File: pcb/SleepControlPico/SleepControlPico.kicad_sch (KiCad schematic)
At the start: 27 parts, among them J1 Display, J2 USB_C_Receptacle_USB2.0, J3 Conn_01x03, J4 Photodiode, SW1 RotaryEncoder_Switch, SW2 Boot, U1 AMS1117-33, U2 ESP32-S3-MINI-1-N8, U3 USBLC6-2SC6

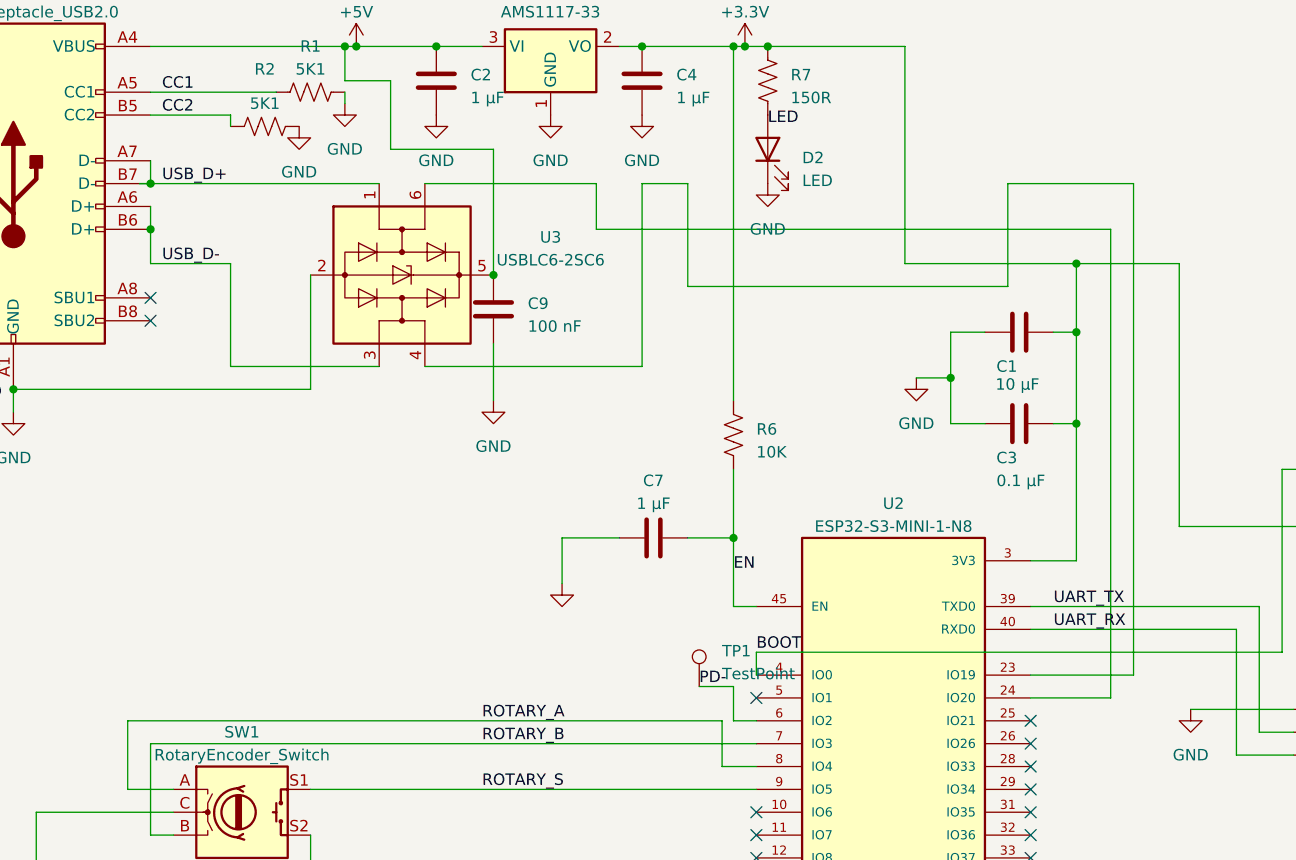
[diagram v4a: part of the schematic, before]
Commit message: Fix USB D+ and D- lines being switched
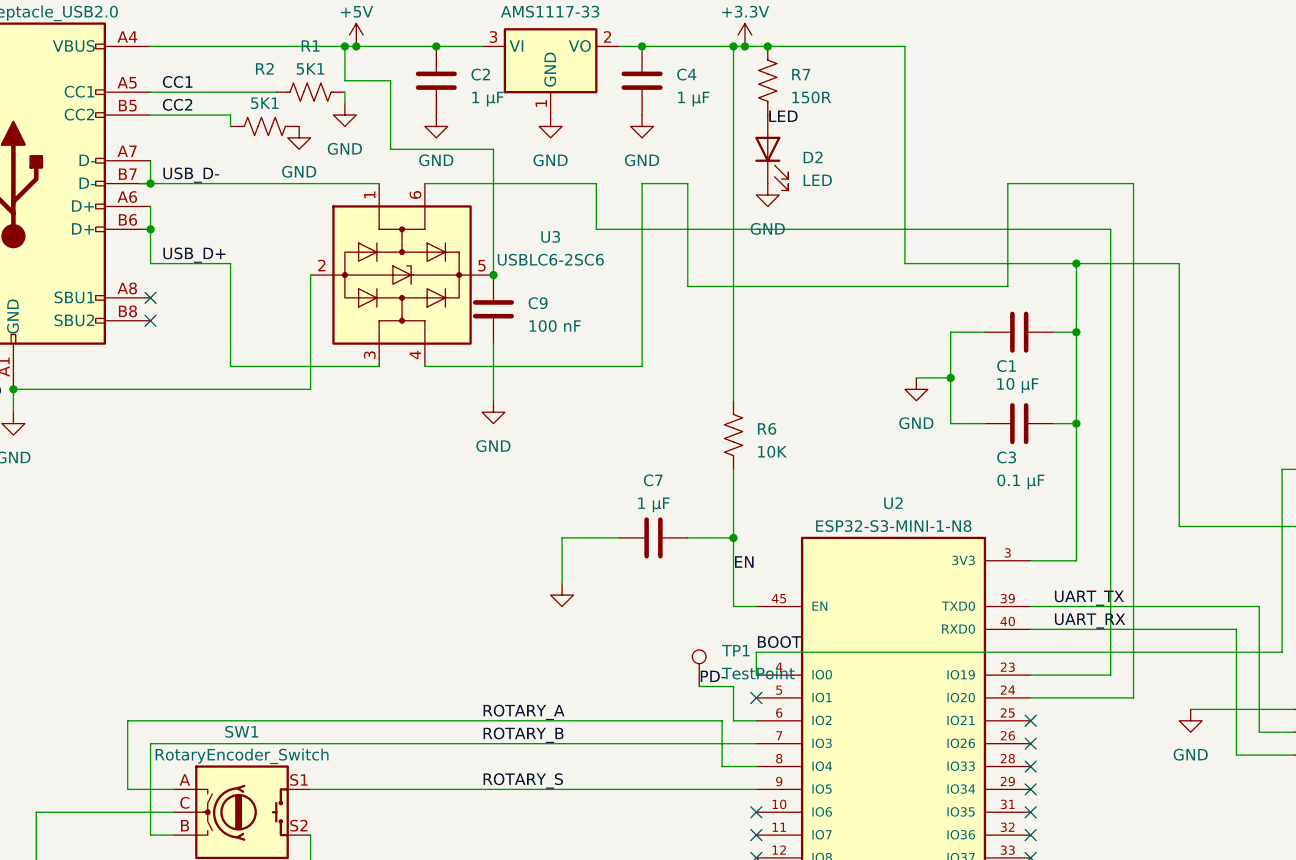
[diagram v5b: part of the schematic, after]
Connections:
- net USB_D+: now also J2.A6 (D+), J2.B6 (D+), U3.3 (I/O2); no longer J2.A7 (D-), J2.B7 (D-), U3.1 (I/O1)
- net USB_D-: now also J2.A7 (D-), J2.B7 (D-), U3.1 (I/O1); no longer J2.A6 (D+), J2.B6 (D+), U3.3 (I/O2)
- net at U2.23 (IO19): now also U3.6 (I/O1); no longer U3.4 (I/O2)
- net at U2.24 (IO20): now also U3.4 (I/O2); no longer U3.6 (I/O1)
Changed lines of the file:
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@@
     (stroke (width 0) (type default))
   )
-  (wire (pts (xy 157.48 49.53) (xy 157.48 101.6))
+  (wire (pts (xy 157.48 49.53) (xy 157.48 99.06))
     (stroke (width 0) (type default))
   )
@@
     (stroke (width 0) (type default))
   )
-  (wire (pts (xy 157.48 101.6) (xy 148.59 101.6))
-    (stroke (width 0) (type default))
-  )
   (wire (pts (xy 189.23 82.55) (xy 190.5 82.55))
     (stroke (width 0) (type default))
@@
     (stroke (width 0) (type default))
   )
-  (wire (pts (xy 160.02 99.06) (xy 148.59 99.06))
-    (stroke (width 0) (type default))
-  )
   (wire (pts (xy 190.5 99.06) (xy 190.5 82.55))
     (stroke (width 0) (type default))
@@
     (stroke (width 0) (type default))
   )
+  (wire (pts (xy 148.59 101.6) (xy 160.02 101.6))
+    (stroke (width 0) (type default))
+  )
   (wire (pts (xy 96.52 83.82) (xy 96.52 88.9))
     (stroke (width 0) (type default))
@@
     (stroke (width 0) (type default))
   )
-  (wire (pts (xy 160.02 44.45) (xy 160.02 99.06))
+  (wire (pts (xy 160.02 44.45) (xy 160.02 101.6))
     (stroke (width 0) (type default))
   )
@@
     (stroke (width 0) (type default))
   )
+  (wire (pts (xy 148.59 99.06) (xy 157.48 99.06))
+    (stroke (width 0) (type default))
+  )
   (wire (pts (xy 99.06 142.24) (xy 118.11 142.24))
     (stroke (width 0) (type default))
@@
     (effects (font (size 1.27 1.27)) (justify left bottom))
   )
-  (label "USB_D-" (at 52.07 53.34 0) (fields_autoplaced)
+  (label "USB_D+" (at 52.07 53.34 0) (fields_autoplaced)
     (effects (font (size 1.27 1.27)) (justify left bottom))
   )
@@
     (effects (font (size 1.27 1.27)) (justify left bottom))
   )
-  (label "USB_D+" (at 52.07 44.45 0) (fields_autoplaced)
-    (effects (font (size 1.27 1.27)) (justify left bottom))
-  )
+  (label "USB_D-" (at 52.07 44.45 0) (fields_autoplaced)
+    (effects (font (size 1.27 1.27)) (justify left bottom))
+  )
